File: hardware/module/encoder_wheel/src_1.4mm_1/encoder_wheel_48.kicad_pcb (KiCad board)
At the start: 2 copper layers, 74 x 74 mm, 2 parts

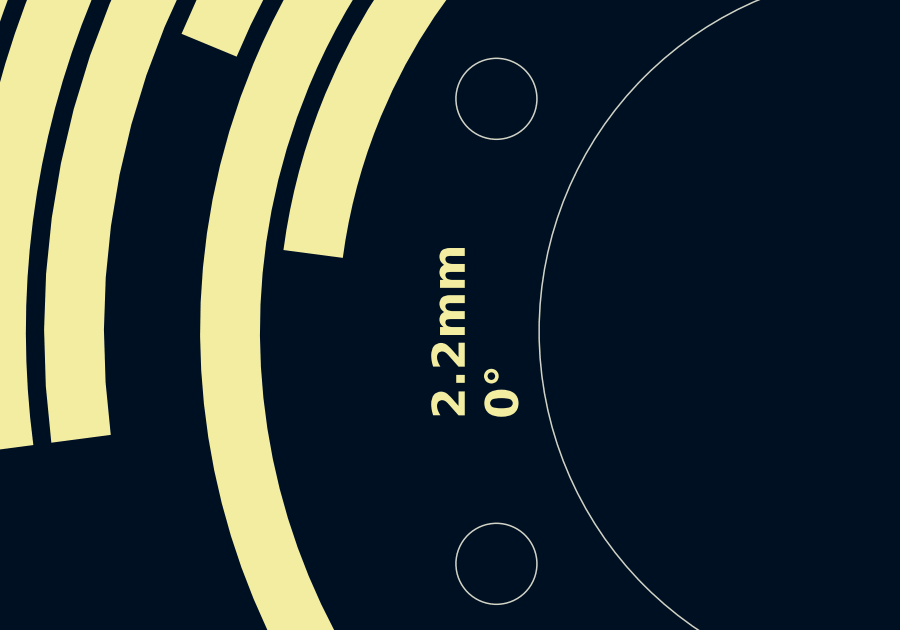
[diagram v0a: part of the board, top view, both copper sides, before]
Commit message: add encoder wheel variants
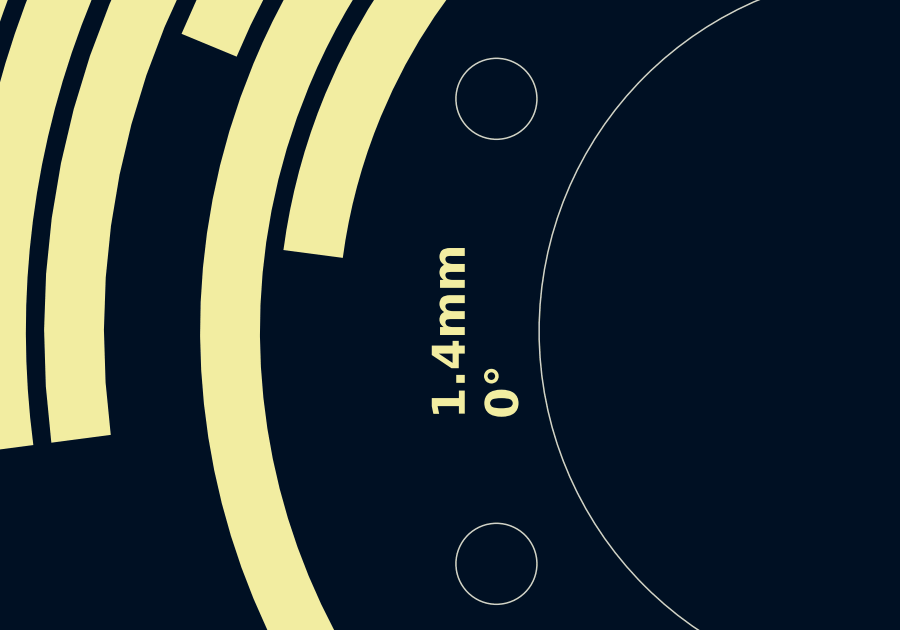
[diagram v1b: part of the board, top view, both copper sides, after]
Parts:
- REF** (x2): value OpenFlapEncoderPattern48_2.2mm -> OpenFlapEncoderPattern48_1.4mm; footprint EncoderPattern:OpenFlapEncoderPattern48_2.2mm -> EncoderPattern:OpenFlapEncoderPattern48_1.4mm
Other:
- board text added: "1.4mm 0°"
- board text added: "1.4mm 3.75°"
- board text removed: "2.2mm 0°"
- board text removed: "2.2mm 3.75°"
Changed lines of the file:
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@@
 	)
 	(net 0 "")
-	(footprint "EncoderPattern:OpenFlapEncoderPattern48_2.2mm"
+	(footprint "EncoderPattern:OpenFlapEncoderPattern48_1.4mm"
 		(layer "F.Cu")
 		(at 101 100)
@@
 			)
 		)
-		(property "Value" "OpenFlapEncoderPattern48_2.2mm"
+		(property "Value" "OpenFlapEncoderPattern48_1.4mm"
 			(at 0 1 0)
 			(unlocked yes)
@@
 			)
 		)
-		(property "Footprint" "EncoderPattern:OpenFlapEncoderPattern48_2.2mm"
+		(property "Footprint" "EncoderPattern:OpenFlapEncoderPattern48_1.4mm"
 			(at 0 0 0)
 			(unlocked yes)
@@
 		)
 	)
-	(footprint "EncoderPattern:OpenFlapEncoderPattern48_2.2mm"
+	(footprint "EncoderPattern:OpenFlapEncoderPattern48_1.4mm"
 		(layer "B.Cu")
 		(at 101 100 -176.25)
@@
 			)
 		)
-		(property "Value" "OpenFlapEncoderPattern48_2.2mm"
+		(property "Value" "OpenFlapEncoderPattern48_1.4mm"
 			(at 0 -1 3.75)
 			(unlocked yes)
@@
 			)
 		)
-		(property "Footprint" "EncoderPattern:OpenFlapEncoderPattern48_2.2mm"
+		(property "Footprint" "EncoderPattern:OpenFlapEncoderPattern48_1.4mm"
 			(at 0 0 3.75)
 			(unlocked yes)
@@
 		(layer "Edge.Cuts")
 	)
-	(gr_text "2.2mm \n3.75°"
+	(gr_text "1.4mm \n3.75°"
 		(at 88.427 97.333 90)
 		(layer "B.SilkS")
@@
 		)
 	)
-	(gr_text "2.2mm \n0°"
+	(gr_text "1.4mm \n0°"
 		(at 88.427 102.921 90)
 		(layer "F.SilkS")

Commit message: encoder changes
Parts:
- renumbered REF** to ENC1, REF** to ENC2

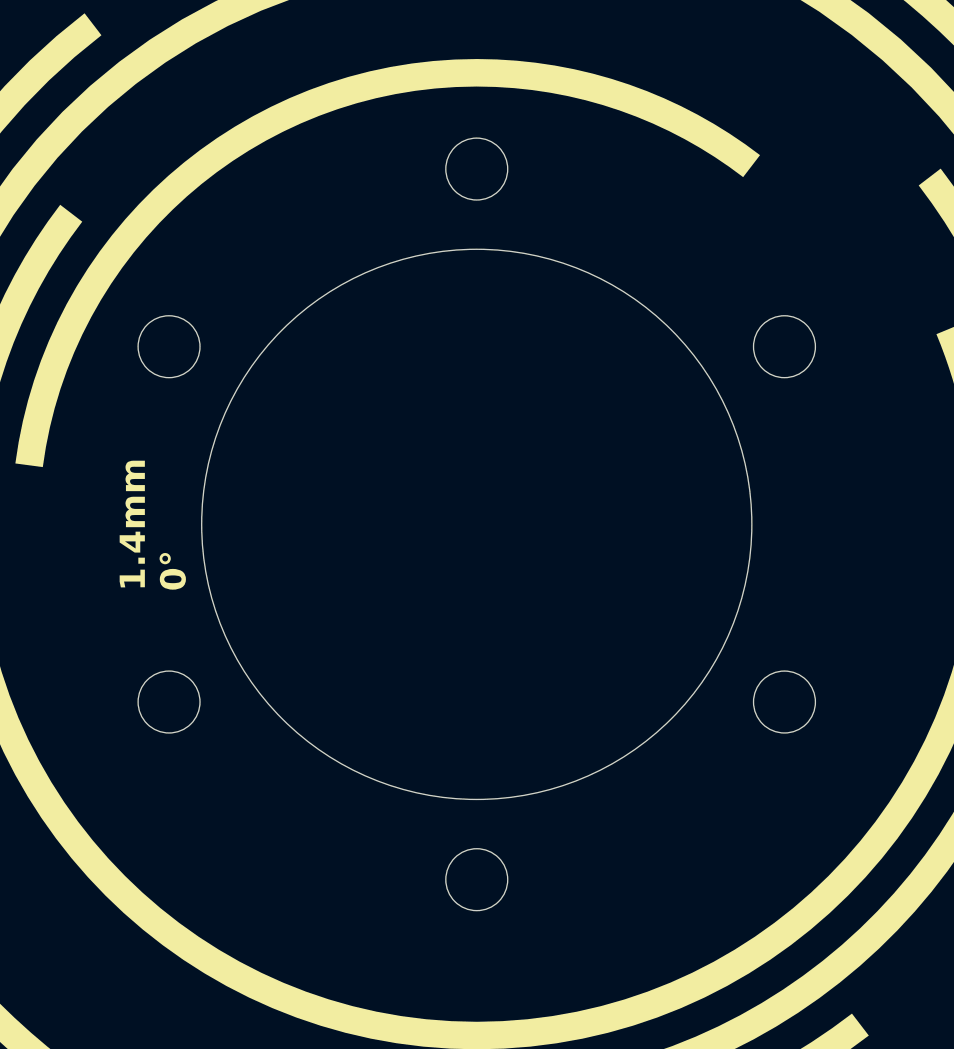
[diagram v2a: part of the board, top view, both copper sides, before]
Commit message: changed hole patern encoder wheel
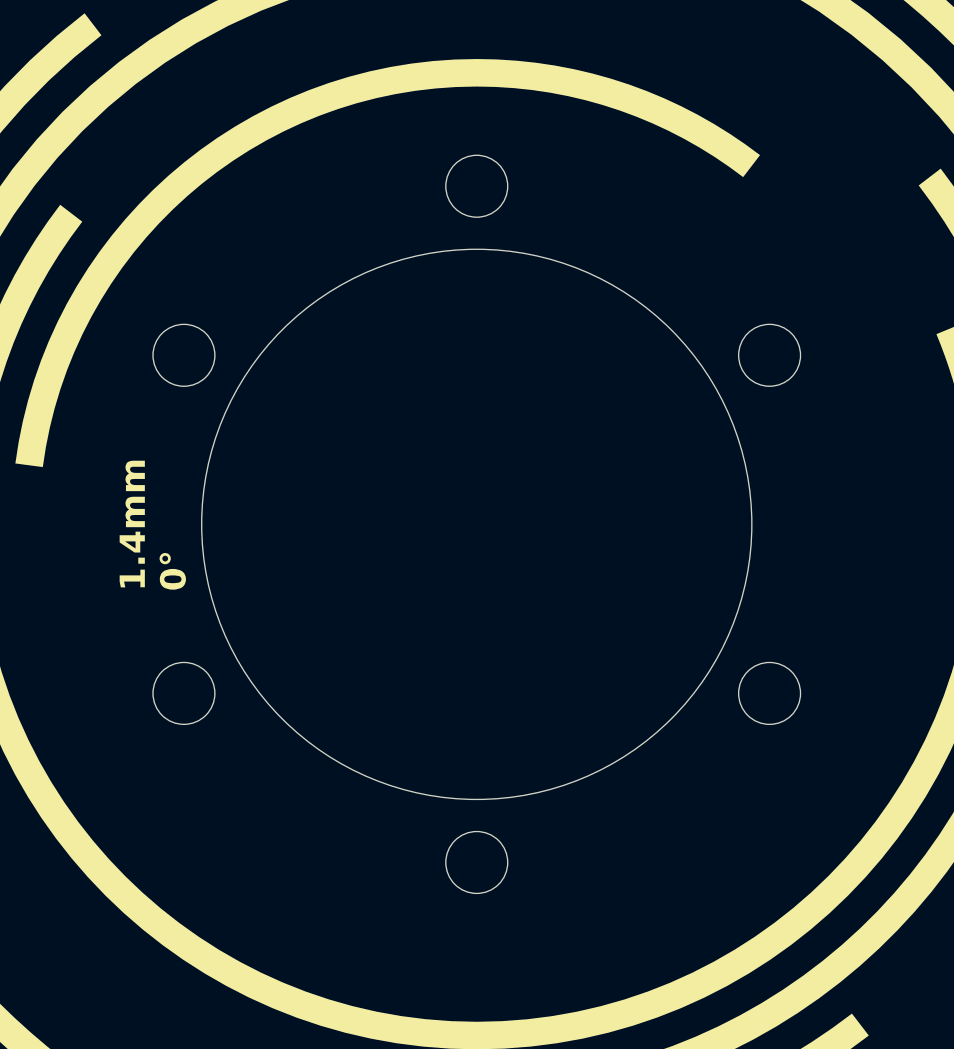
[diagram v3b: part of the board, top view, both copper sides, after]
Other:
- outline, holes or cut-outs redrawn
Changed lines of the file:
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@@
 				(xy -29.648512 12.312779) (xy -30.035695 11.33664) (xy -30.391591 10.345177) (xy -30.715618 9.339012)
 				(xy -31.00719 8.318767) (xy -32.16991 8.630376) (xy -31.867817 9.689404) (xy -31.532072 10.733753)
-				(xy -31.163275 11.762782) (xy -30.762029 12.775851) (xy -30.328927 13.77232) (xy -29.864578 14.751548)
+				(xy -31.163275 11.762782) (xy -30.76203 12.775851) (xy -30.328927 13.77232) (xy -29.864578 14.751548)
 				(xy -29.36958 15.712897) (xy -28.844532 16.655725)
 			)
@@
 				(xy 23.399306 17.956937) (xy 22.800573 18.710121) (xy 22.178122 19.443069) (xy 21.532533 20.1552)
 				(xy 20.864385 20.845935) (xy 20.174256 21.514693) (xy 19.462726 22.160893) (xy 18.730374 22.783956)
-				(xy 17.977778 23.383301) (xy 17.205518 23.958347) (xy 16.414174 24.508514) (xy 15.604319 25.033222)
+				(xy 17.977778 23.383301) (xy 17.205518 23.958347) (xy 16.414175 24.508514) (xy 15.604319 25.033222)
 				(xy 14.776538 25.531891) (xy 13.931409 26.003939) (xy 13.06951 26.448787) (xy 12.191419 26.865855)
 				(xy 11.297717 27.254561) (xy 11.758673 28.367155)
@@
 				(xy -16.249198 26.05277) (xy -15.400388 26.564245) (xy -14.534001 27.048825) (xy -13.650611 27.505931)
 				(xy -12.750792 27.934986) (xy -11.835118 28.335413) (xy -10.904163 28.706633) (xy -9.9585 29.048069)
-				(xy -8.998703 29.359143) (xy -8.025348 29.639277) (xy -7.039006 29.887894) (xy -6.040252 30.104418)
+				(xy -8.998703 29.359143) (xy -8.025348 29.639277) (xy -7.039006 29.887894) (xy -6.040252 30.104419)
 				(xy -5.029661 30.288264) (xy -4.007806 30.438862)
 			)
@@
 		(fp_poly
 			(pts
-				(xy -16.372943 21.337093) (xy -17.545687 20.382265) (xy -18.662484 19.364281) (xy -19.720615 18.285859)
+				(xy -16.372943 21.337093) (xy -17.545687 20.382265) (xy -18.662484 19.364281) (xy -19.720615 18.285861)
 				(xy -20.71736 17.149698) (xy -21.649997 15.958522) (xy -22.515808 14.715038) (xy -23.31207 13.421959)
 				(xy -24.036065 12.081996) (xy -24.685072 10.697861) (xy -25.25637 9.272266) (xy -25.74724 7.807923)
@@
 				(xy -26.842306 -1.767383) (xy -26.810194 -2.204587) (xy -26.771152 -2.63984) (xy -26.725252 -3.07309)
 				(xy -26.672571 -3.504284) (xy -27.862163 -3.660863) (xy -27.917046 -3.210451) (xy -27.964894 -2.757881)
-				(xy -28.005618 -2.303205) (xy -28.039133 -1.846481) (xy -28.065351 -1.387751) (xy -28.084186 -0.927077)
+				(xy -28.005618 -2.303205) (xy -28.039133 -1.846483) (xy -28.065351 -1.387751) (xy -28.084186 -0.927077)
 				(xy -28.09555 -0.464511) (xy -28.099358 -0.000104) (xy -28.049356 1.691358) (xy -27.901235 3.356237)
 				(xy -27.657822 4.991716) (xy -27.321945 6.594975) (xy -26.896431 8.163197) (xy -26.384106 9.693563)
@@
 				(xy 17.102531 -22.300553) (xy 16.200668 -22.964999) (xy 15.271869 -23.593882) (xy 14.317133 -24.186193)
 				(xy 13.337458 -24.740925) (xy 12.333847 -25.257069) (xy 11.307298 -25.733618) (xy 10.258811 -26.169565)
-				(xy 9.189386 -26.563901) (xy 8.100023 -26.915619) (xy 6.991723 -27.223713) (xy 5.865484 -27.487168)
+				(xy 9.189386 -26.563901) (xy 8.100023 -26.915619) (xy 6.991723 -27.223715) (xy 5.865484 -27.487168)
 				(xy 4.722307 -27.704985) (xy 3.563192 -27.876152) (xy 2.389139 -27.999661) (xy 1.201147 -28.074506)
 				(xy 0.000217 -28.099679) (xy -0.712155 -28.090827) (xy -1.420125 -28.064413) (xy -2.123489 -28.020648)
@@
 				(xy -15.400696 -16.954222) (xy -16.195837 -16.196159) (xy -16.953901 -15.401018) (xy -17.673453 -14.570236)
 				(xy -18.353059 -13.705245) (xy -18.991285 -12.80748) (xy -19.586696 -11.878376) (xy -20.137858 -10.919368)
-				(xy -20.643337 -9.931889) (xy -21.101697 -8.917374) (xy -21.511504 -7.877262) (xy -21.871325 -6.812976)
-				(xy -22.179724 -5.725961) (xy -22.435268 -4.617647) (xy -22.63652 -3.489471) (xy -22.782048 -2.342868)
+				(xy -20.643337 -9.931889) (xy -21.101697 -8.917374) (xy -21.511504 -7.877263) (xy -21.871325 -6.812976)
+				(xy -22.179724 -5.725961) (xy -22.435268 -4.617647) (xy -22.63652 -3.489471) (xy -22.782048 -2.34287)
 				(xy -22.870417 -1.179264) (xy -22.900192 -0.000104) (xy -22.879662 0.978991) (xy -22.81862 1.947526)
 				(xy -22.71789 2.904685) (xy -22.578294 3.849654) (xy -22.400657 4.781617) (xy -22.1858 5.699759)
 				(xy -21.934547 6.603265) (xy -21.647722 7.491319) (xy -21.326147 8.363107) (xy -20.970646 9.217813)
 				(xy -20.582042 10.054622) (xy -20.161157 10.872718) (xy -19.708816 11.671288) (xy -19.225841 12.449514)
-				(xy -18.713056 13.206583) (xy -18.171286 13.941678)
+				(xy -18.713056 13.206583) (xy -18.171287 13.941678)
 			)
 			(stroke
@@
 	)
 	(gr_circle
-		(center 87.576606 107.75)
-		(end 88.926606 107.75)
+		(center 88.226125 107.375)
+		(end 89.576125 107.375)
 		(stroke
 			(width 0.05)
@@
 	)
 	(gr_circle
-		(center 101 84.5)
-		(end 102.35 84.5)
-		(stroke
-			(width 0.05)
-			(type default)
-		)
-		(fill none)
-		(layer "Edge.Cuts")
-	)
-	(gr_circle
-		(center 114.423394 92.25)
-		(end 115.773394 92.25)
-		(stroke
-			(width 0.05)
-			(type default)
-		)
-		(fill none)
-		(layer "Edge.Cuts")
-	)
-	(gr_circle
-		(center 87.576606 92.25)
-		(end 88.926606 92.25)
+		(center 101 85.25)
+		(end 102.35 85.25)
+		(stroke
+			(width 0.05)
+			(type default)
+		)
+		(fill none)
+		(layer "Edge.Cuts")
+	)
+	(gr_circle
+		(center 113.773875 92.625)
+		(end 115.123875 92.625)
+		(stroke
+			(width 0.05)
+			(type default)
+		)
+		(fill none)
+		(layer "Edge.Cuts")
+	)
+	(gr_circle
+		(center 88.226125 92.625)
+		(end 89.576125 92.625)
 		(stroke
 			(width 0.05)
@@
 	)
 	(gr_circle
-		(center 114.423394 107.75)
-		(end 115.773394 107.75)
-		(stroke
-			(width 0.05)
-			(type default)
-		)
-		(fill none)
-		(layer "Edge.Cuts")
-	)
-	(gr_circle
-		(center 101 115.5)
-		(end 102.35 115.5)
-		(stroke
-			(width 0.05)
+		(center 113.773875 107.375)
+		(end 115.123875 107.375)
+		(stroke
+			(width 0.05)
+			(type default)
+		)
+		(fill none)
+		(layer "Edge.Cuts")
+	)
+	(gr_circle
+		(center 101 114.75)
+		(end 102.35 114.75)
+		(stroke
+			(width 0.05)
